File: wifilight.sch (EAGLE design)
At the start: 36 parts, among them Q1 BUK98180-100A, Q2 BUK98180-100A, Q3 BUK98180-100A, Q4 BUK98180-100A, U1 TCA6507PW, X1 53261-06

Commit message: Made mofications to schematics for readability
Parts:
- added FRAME1: (no value), SparkFun-Aesthetics:FRAME-LETTERNO_PACKAGE
- added LOGO1: OSHW-LOGOS, SparkFun-Aesthetics:OSHW-LOGOS
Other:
- note added: "Diagnostic LEDs + Programming Port"
- note added: "LED Drivers"
- note added: "LEDs"
- note added: "Microcontroller + PWM Generator + Pullups"
- note added: "Power Rectification and Voltage Regulation"
- moved on the sheet: B2, C1, C2, C3, C5, C6, C7, CN1, LED1, LED2, LED3, LED4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

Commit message: Revised to use larger regulators, Revised to use 4 layers
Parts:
- removed C3: (no value), rcl:CPOL-EUE3.5-8
- removed REG2: MC33269-SO8, linear:MC33269-SO8
- added C4: 0.1uF, SparkFun-Passives:CAP1206
- added C8: 10uF, SparkFun-Passives:CAP1206
- added IC1, IC2: REG1117, burr-brown:REG1117
- renumbered PWR to POWER
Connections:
- new net 5V: C4.1, C8.1, IC1.VOUT, IC2.VIN
- net 12V: now also IC1.VIN; no longer C3.+, REG2.IN
- net 3.3V: now also IC2.VOUT; no longer REG2.OUT, REG2.OUT@1, REG2.OUT@2, REG2.OUT@3
- net GND: now also C4.2, C8.2; no longer C3.-, REG2.GND/ADJ
- net RXD: now also X1-1.S; no longer X1-2.S
- net TXD: now also X1-2.S; no longer X1-1.S
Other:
- moved on the sheet: C5, C6, C7

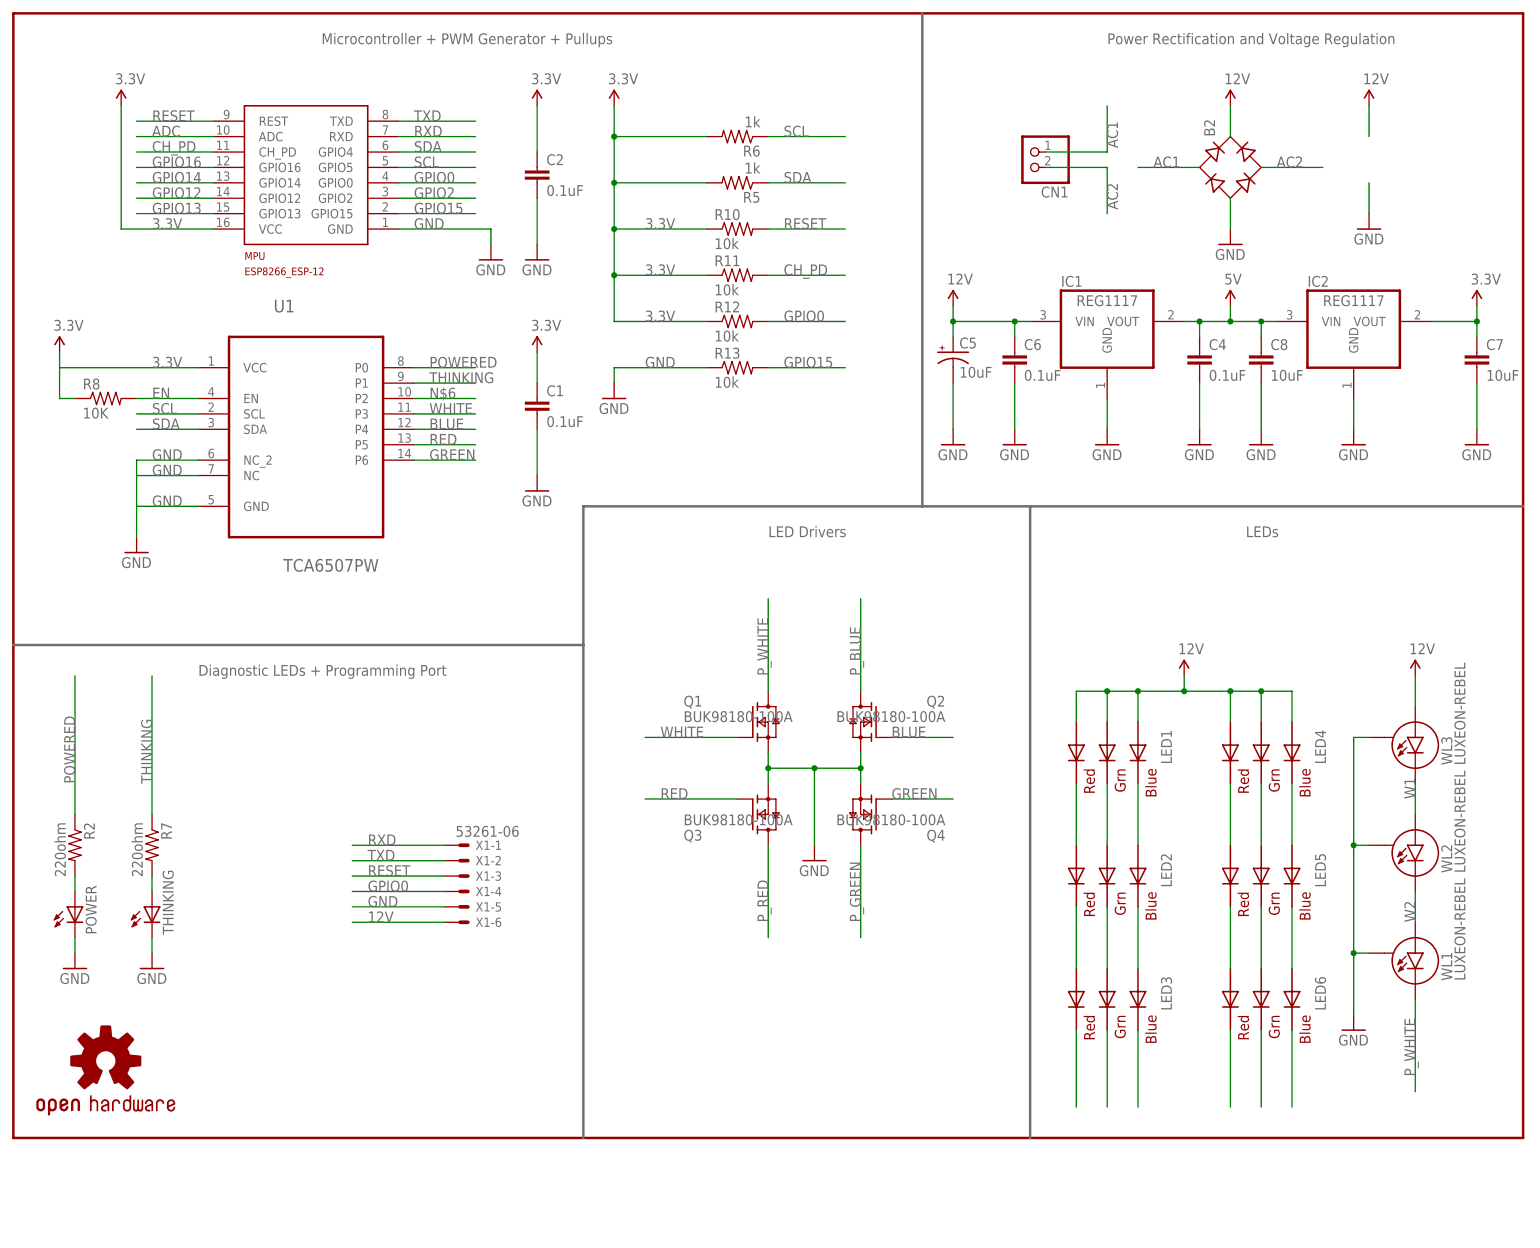
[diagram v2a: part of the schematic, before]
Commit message: Mk8 gets its PCA9685 back, the older LED controller turned out to only have 2 channels of PWM available, which is insufficient. Respan this board with 3xRGB 5050's and 3xLuxeon rebels. reduced complexity lets us have 2 layer boards again. Almost everything 'cept the MCU is on the front, save for 4 resistors and the programming harness. May still have to flip RX & TX
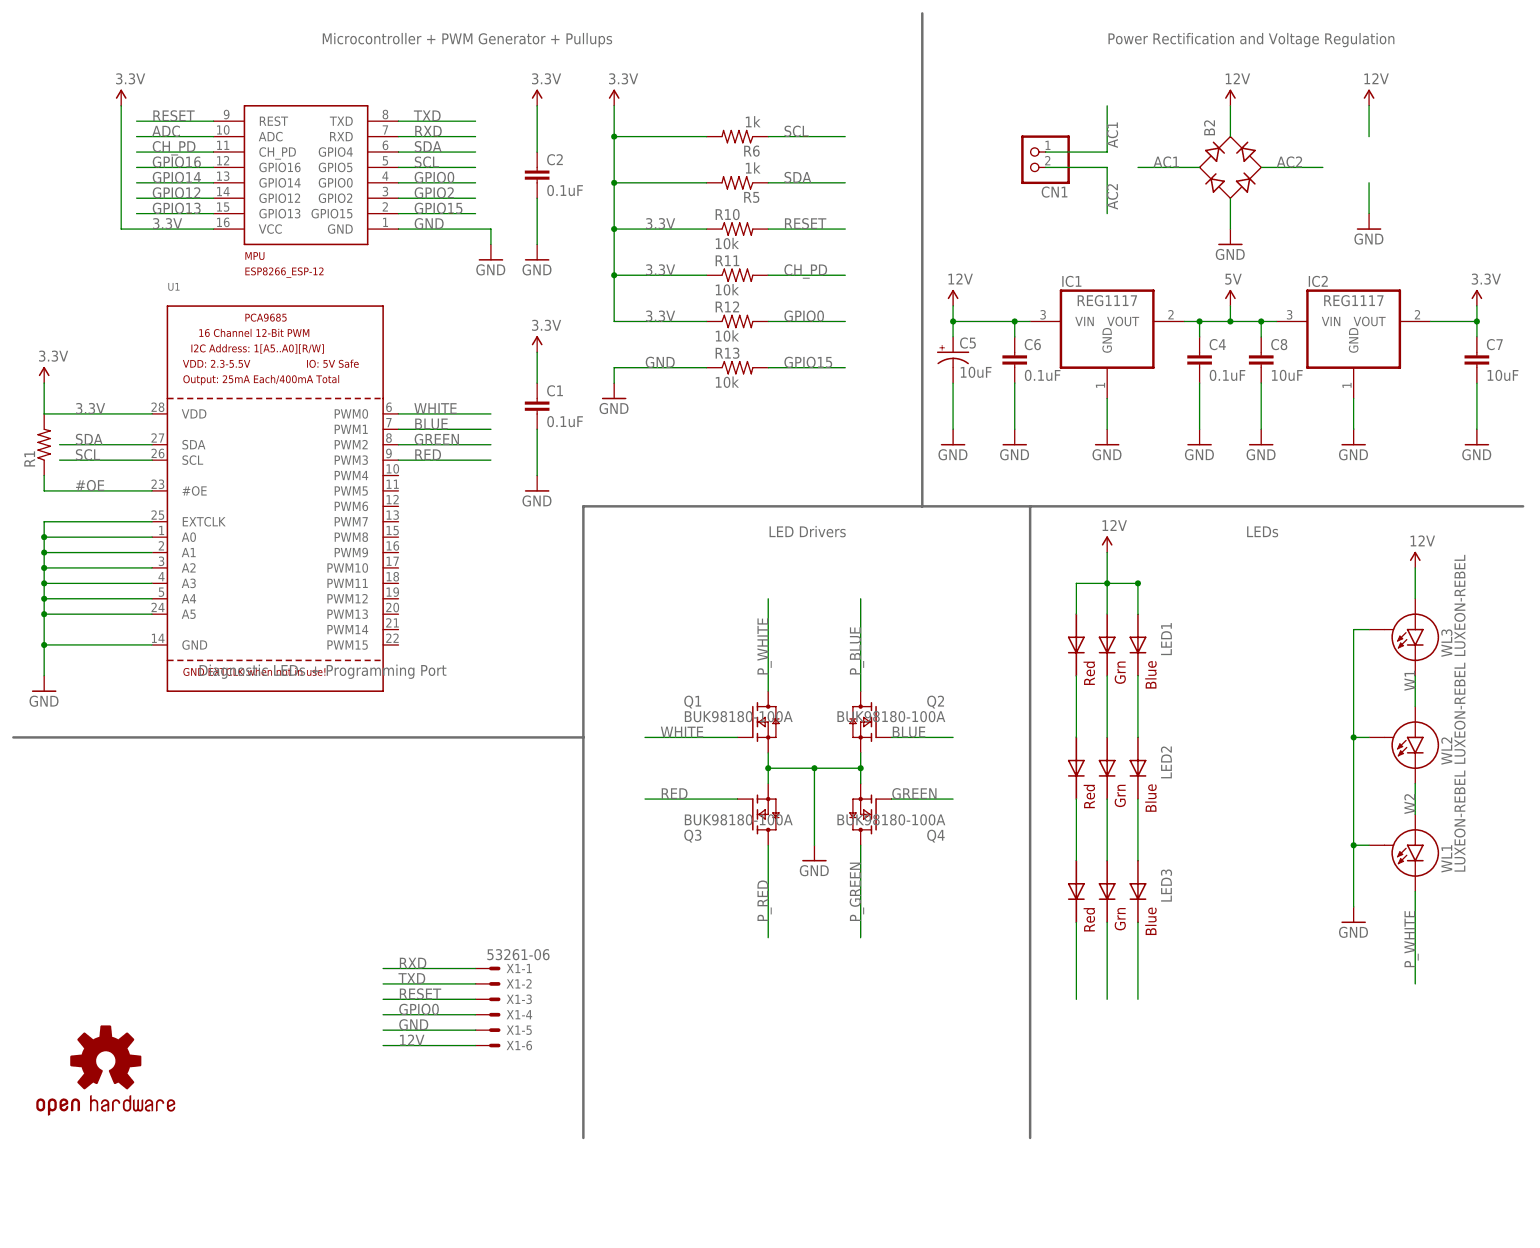
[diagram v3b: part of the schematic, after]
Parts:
- removed FRAME1: (no value), SparkFun-Aesthetics:FRAME-LETTERNO_PACKAGE
- removed LED4, LED5, LED6: RGBLED5050, adafruit:RGBLED5050
- removed POWER, THINKING: (no value), led:LEDCHIP-LED0805
- removed R2, R7: 220ohm, SparkFun-Passives:RESISTOR1206
- removed R8: 10K, SparkFun-Passives:RESISTOR1206
- added R1: (no value), SparkFun-Resistors:RESISTOR1206
- U1: value TCA6507PW -> (none); device Texas Instruments_By_element14_Batch_1:TCA6507PW -> adafruit:PCA9685
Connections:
- removed net EN: R8.2, U1.EN
- removed net N$14: POWER.A, R2.2
- removed net N$15: R7.2, THINKING.A
- removed net N$37: LED4.RED_C, LED5.RED_A
- removed net N$38: LED4.GREEN_C, LED5.GREEN_A
- removed net N$39: LED4.BLUE_C, LED5.BLUE_A
- removed net N$40: LED5.RED_C, LED6.RED_A
- removed net N$41: LED5.GREEN_C, LED6.GREEN_A
- removed net N$42: LED5.BLUE_C, LED6.BLUE_A
- removed net N$6: U1.P2
- removed net POWERED: R2.1, U1.P0
- removed net THINKING: R7.1, U1.P1
- new net #OE: R1.1, U1.#OE
- net 12V: no longer LED4.BLUE_A, LED4.GREEN_A, LED4.RED_A
- net 3.3V: now also R1.2, U1.VDD; no longer R8.1, U1.VCC
- net BLUE: now also U1.PWM1; no longer U1.P4
- net GND: now also U1.A0, U1.A1, U1.A2, U1.A3, U1.A4, U1.A5, U1.EXTCLK; no longer POWER.C, THINKING.C, U1.NC, U1.NC_2
- net GREEN: now also U1.PWM2; no longer U1.P6
- net P_BLUE: no longer LED6.BLUE_C
- net P_GREEN: no longer LED6.GREEN_C
- net P_RED: no longer LED6.RED_C
- net RED: now also U1.PWM3; no longer U1.P5
- net WHITE: now also U1.PWM0; no longer U1.P3
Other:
- moved on the sheet: LED1, LED2, LED3, WL1, WL2, WL3, X1-1, X1-2, X1-3, X1-4, X1-5, X1-6

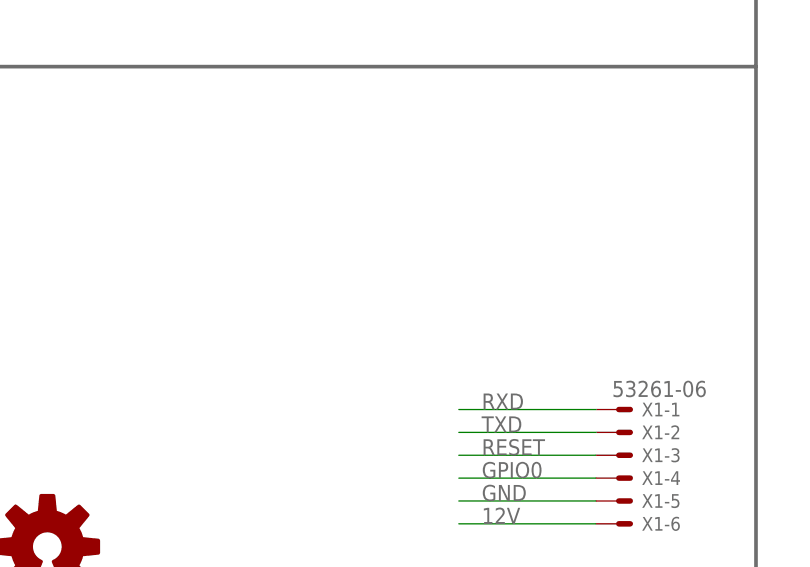
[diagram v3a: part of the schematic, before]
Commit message: Add ICSP header. Resolves #5
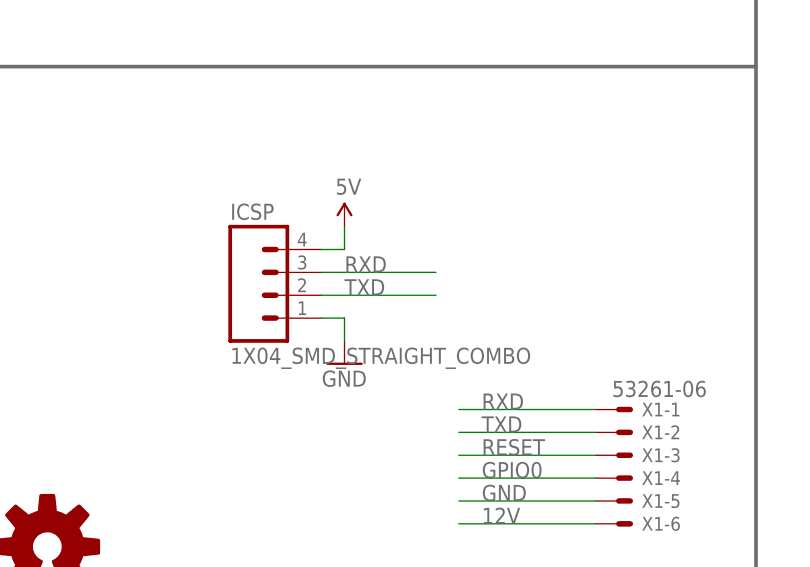
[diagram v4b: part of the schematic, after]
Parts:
- added ICSP: 1X04_SMD_STRAIGHT_COMBO, SparkFun-Connectors:M04SMD_STRAIGHT_COMBO
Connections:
- net 5V: now also ICSP.4
- net GND: now also ICSP.1
- net RXD: now also ICSP.3
- net TXD: now also ICSP.2
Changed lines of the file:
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@@
 <part name="GND3" library="SparkFun-Aesthetics" deviceset="GND" device=""/>
 <part name="FRAME2" library="SparkFun-Aesthetics" deviceset="FRAME-A4L" device=""/>
+<part name="SUPPLY11" library="SparkFun-Aesthetics" deviceset="5V" device=""/>
+<part name="GND6" library="SparkFun-Aesthetics" deviceset="GND" device=""/>
+<part name="ICSP" library="SparkFun-Connectors" deviceset="M04" device="SMD_STRAIGHT_COMBO" value="1X04_SMD_STRAIGHT_COMBO"/>
 </parts>
 <sheets>
@@
 <instance part="GND3" gate="1" x="5.08" y="73.66"/>
 <instance part="FRAME2" gate="G$1" x="0" y="0"/>
+<instance part="SUPPLY11" gate="G$1" x="48.26" y="48.26"/>
+<instance part="GND6" gate="1" x="48.26" y="33.02"/>
+<instance part="ICSP" gate="G$1" x="40.64" y="40.64"/>
 </instances>
 <busses>
@@
 <junction x="5.08" y="81.28"/>
 </segment>
+<segment>
+<wire x1="45.72" y1="38.1" x2="48.26" y2="38.1" width="0.1524" layer="91"/>
+<wire x1="48.26" y1="38.1" x2="48.26" y2="35.56" width="0.1524" layer="91"/>
+<pinref part="GND6" gate="1" pin="GND"/>
+<pinref part="ICSP" gate="G$1" pin="1"/>
+</segment>
 </net>
 <net name="SCL" class="0">
@@
 <label x="63.5" y="25.4" size="1.778" layer="95"/>
 </segment>
+<segment>
+<wire x1="58.42" y1="40.64" x2="45.72" y2="40.64" width="0.1524" layer="91"/>
+<label x="48.26" y="40.64" size="1.778" layer="95"/>
+<pinref part="ICSP" gate="G$1" pin="2"/>
+</segment>
 </net>
 <net name="RXD" class="0">
@@
 <wire x1="76.2" y1="27.94" x2="60.96" y2="27.94" width="0.1524" layer="91"/>
 <label x="63.5" y="27.94" size="1.778" layer="95"/>
+</segment>
+<segment>
+<wire x1="45.72" y1="43.18" x2="58.42" y2="43.18" width="0.1524" layer="91"/>
+<label x="48.26" y="43.18" size="1.778" layer="95"/>
+<pinref part="ICSP" gate="G$1" pin="3"/>
 </segment>
 </net>
@@
 <junction x="200.66" y="134.62"/>
 </segment>
-</net>
+<segment>
+<wire x1="45.72" y1="45.72" x2="48.26" y2="45.72" width="0.1524" layer="91"/>
+<wire x1="48.26" y1="45.72" x2="48.26" y2="48.26" width="0.1524" layer="91"/>
+<pinref part="SUPPLY11" gate="G$1" pin="5V"/>
+<pinref part="ICSP" gate="G$1" pin="4"/>
+</segment>
+</net>
